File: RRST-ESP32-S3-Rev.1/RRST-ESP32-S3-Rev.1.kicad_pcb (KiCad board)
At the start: 2 copper layers, 25.4 x 62.7 mm, 29 parts, among them J1 Conn_01x22_Pin, J2 USB_C_Receptacle_USB2.0_16P, J3 Conn_01x22_Pin, SW1 SW_Push, SW2 SW_Push, U1 ESP32-S3-WROOM-1, U2 LD1117S33TR_SOT223

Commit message: 製造ファイル出力
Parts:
- added G***: LOGO, LOGO, F.Cu at (82.8, 125.5)
- added G***: LOGO, LOGO, F.Cu at (84.6, 102.9)
- added G***: LOGO, LOGO, B.Cu at (86.4, 105.2)
- added G***: LOGO, LOGO, B.Cu at (79.1, 104.5)
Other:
- board text added: "RRST-ESP32-S3 Rev.1 2026, NHK-Project, RRST"

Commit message: シルクやり直し
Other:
- board text added: "3.3V"
- board text added: "5V"
- board text added: "BOOT"
- board text added: "LED"
- board text added: "RESET"
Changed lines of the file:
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@@
 		(layer "Edge.Cuts")
+	)
+	(gr_text "3.3V"
+		(at 88.8238 113.411 0)
+		(layer "F.SilkS" knockout)
+		(effects
+			(font
+				(size 1 1)
+				(thickness 0.2)
+				(bold yes)
+			)
+			(justify left bottom)
+		)
+	)
+	(gr_text "5V"
+		(at 88.773 123.571 0)
+		(layer "F.SilkS" knockout)
+		(effects
+			(font
+				(size 1 1)
+				(thickness 0.2)
+				(bold yes)
+			)
+			(justify left bottom)
+		)
+	)
+	(gr_text "RESET"
+		(at 78.5368 111.379 0)
+		(layer "F.SilkS" knockout)
+		(effects
+			(font
+				(size 1 1)
+				(thickness 0.2)
+				(bold yes)
+			)
+			(justify left bottom)
+		)
+	)
+	(gr_text "BOOT"
+		(at 87.0966 111.379 0)
+		(layer "F.SilkS" knockout)
+		(effects
+			(font
+				(size 1 1)
+				(thickness 0.2)
+				(bold yes)
+			)
+			(justify left bottom)
+		)
+	)
+	(gr_text "LED"
+		(at 92.1447 99.536 0)
+		(layer "F.SilkS" knockout)
+		(effects
+			(font
+				(size 1 1)
+				(thickness 0.2)
+				(bold yes)
+			)
+			(justify left bottom)
+		)
 	)
 	(gr_text "RRST-ESP32-S3 Rev.1\n2026, NHK-Project, RRST\n"

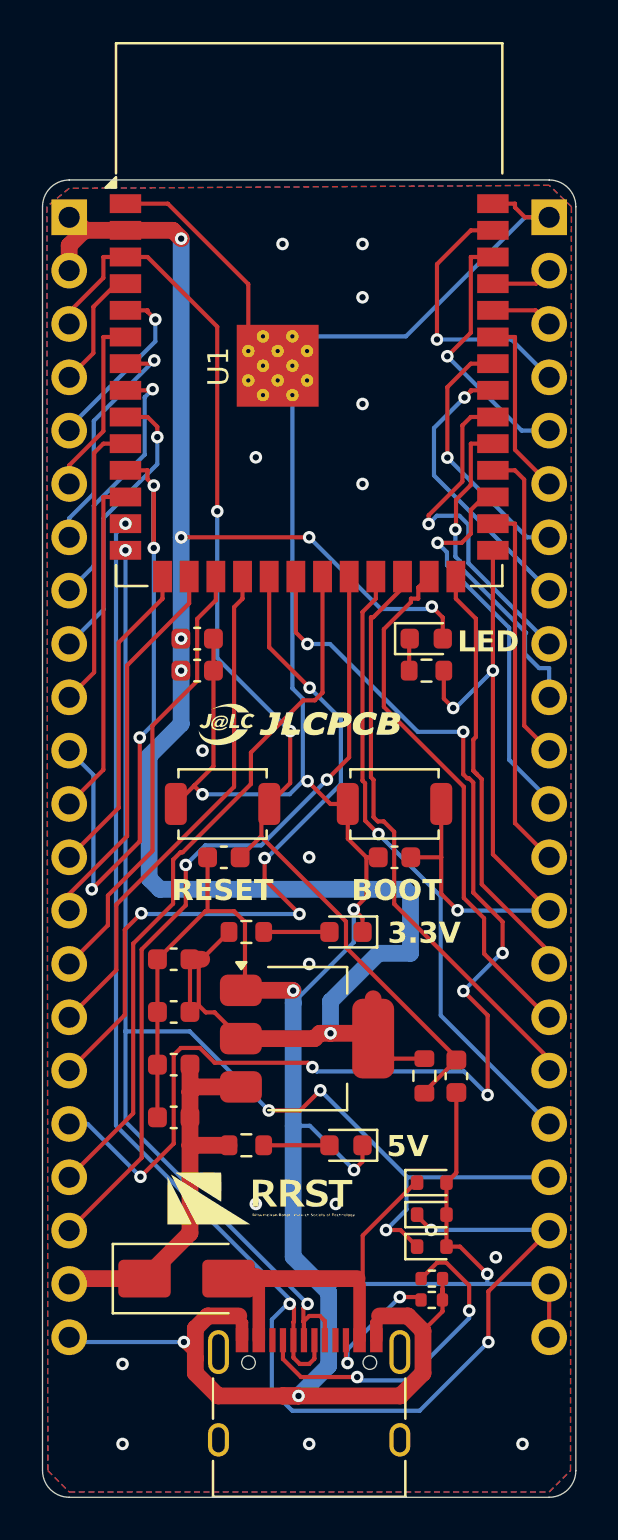
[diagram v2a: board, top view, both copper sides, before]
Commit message: シルクやり直し２
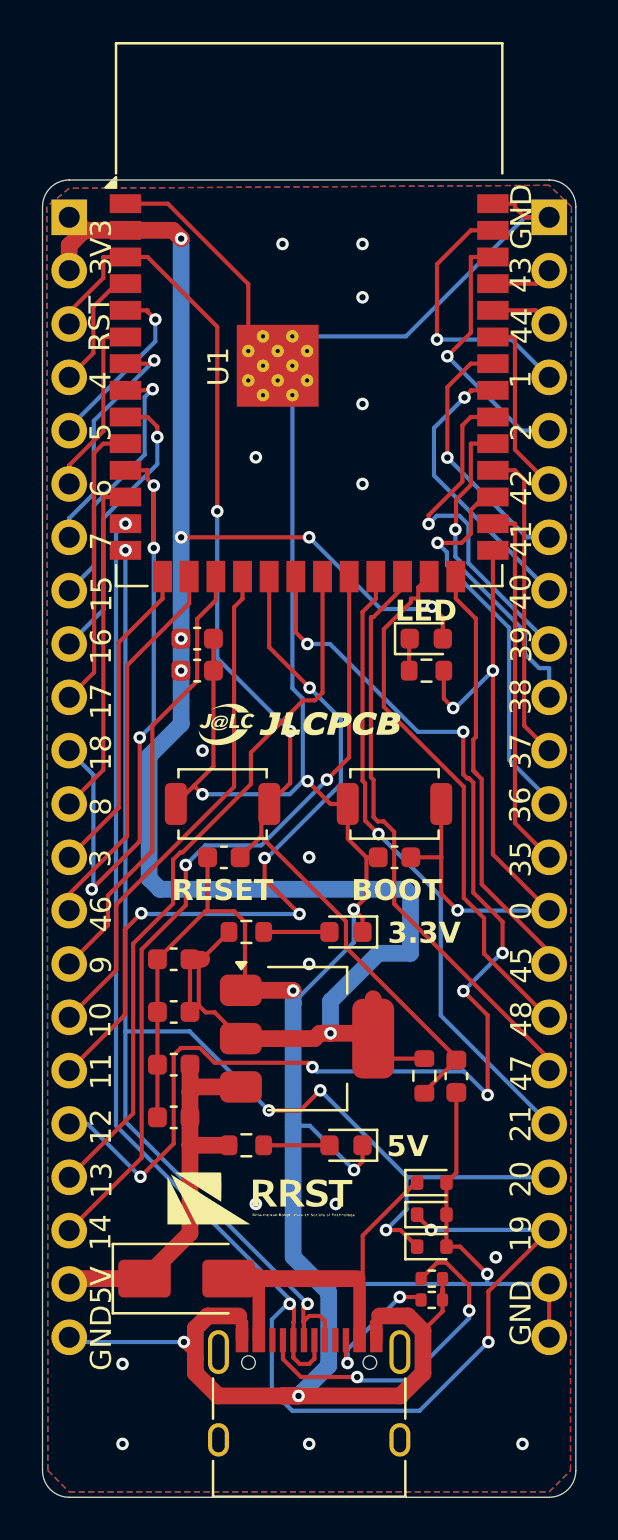
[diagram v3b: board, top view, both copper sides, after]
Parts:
- moved G*** 1.51 mm to (86.2, 106.7)
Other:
- board text added: "0"
- board text added: "1"
- board text added: "10"
- board text added: "11"
- board text added: "12"
- board text added: "13"
- board text added: "14"
- board text added: "15"
- board text added: "16"
- board text added: "17"
- board text added: "18"
- board text added: "19"
- board text added: "2"
- board text added: "20"
- board text added: "21"
- board text added: "3"
- board text added: "35"
- board text added: "36"
- board text added: "37"
- board text added: "38"
- board text added: "39"
- board text added: "3V3"
- board text added: "4"
- board text added: "40"
- board text added: "41"
- board text added: "42"
- board text added: "43"
- board text added: "44"
- board text added: "45"
- board text added: "46"
- board text added: "47"
- board text added: "48"
- board text added: "5"
- board text added: "6"
- board text added: "7"
- board text added: "8"
- board text added: "9"
- board text added: "GND"
- board text added: "RST"

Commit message: 製造ファイル出力3
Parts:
- R3, R4: footprint Resistor_SMD:R_0402_1005Metric -> Resistor_SMD:R_0603_1608Metric
- moved R3 2.07 mm to (92.6, 131.5)
- moved R4 1.82 mm to (92.6, 130.0)
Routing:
- net Net-(J2-CC1): track 16.0 -> 12.8 mm
- net Net-(J2-CC2): track 6.36 -> 8.21 mm
- net DN: track 75.9 -> 76.5 mm
